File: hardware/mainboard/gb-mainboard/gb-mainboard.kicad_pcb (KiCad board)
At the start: 2 copper layers, 77.4 x 81 mm, 0 parts

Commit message: .
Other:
- net class Default: trace_width 0.25 -> 0.15

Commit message: started placing some components
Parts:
- added BRD101: POLOLU-2130, BOARD:POLOLU-2130, F.Cu at (129.1, 78.4)
- added P101: NUCLEO-CN7, CONNECTOR:SOCKET_20x2_2.54-WE-61304021821, F.Cu at (159.3, 92.3)
- added P102: NUCLEO-CN10, CONNECTOR:SOCKET_20x2_2.54-WE-61304021821, F.Cu at (98.4, 92.3)
- added P103: MOTOR_SX, CONNECTOR_MPT:CONN-MPT0.5_2-2.54, F.Cu at (115.0, 78.7)
- added P104: MOTOR_DX, CONNECTOR_MPT:CONN-MPT0.5_2-2.54, F.Cu at (142.6, 78.7)
- added P105: WE-632723300011, CONNECTOR:USB3.1-C_WE-632723300011, F.Cu at (139.8, 130.2)
- added U101: ESP32-WROOM-32E(8MB), WIFI:ESP32-WROOM-32D, F.Cu at (113.5, 125.5)
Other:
- outline, holes or cut-outs redrawn

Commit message: .
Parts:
- moved BRD101 0.49 mm to (128.7, 78.7), turned to 0 degrees
- moved P104 0.38 mm to (142.9, 78.7)
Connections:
- P103 pad 1: Net-(P103-Pad1) -> Net-(BRD101-Pad14)
- P103 pad 2: Net-(P103-Pad2) -> Net-(BRD101-Pad13)
- P104 pad 1: Net-(P104-Pad1) -> Net-(BRD101-Pad11)
- P104 pad 2: Net-(P104-Pad2) -> Net-(BRD101-Pad12)
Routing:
- net Net-(BRD101-Pad13): track 0.00 -> 21.7 mm
- net Net-(BRD101-Pad12): track 0.00 -> 19.4 mm
- net Net-(BRD101-Pad14): track 0.00 -> 12.6 mm
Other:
- net class Default: trace_width 0.15 -> 0.2
- rule via_min_size: 0.4 -> 0.6

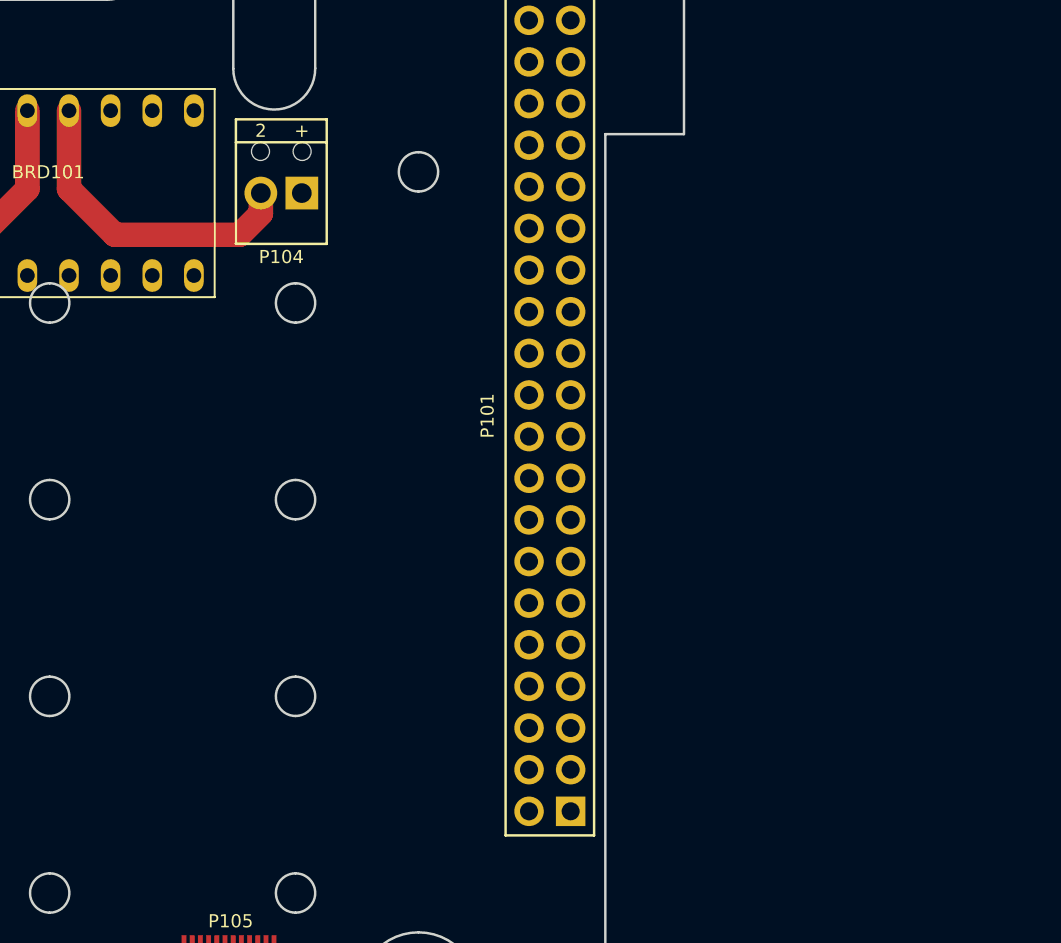
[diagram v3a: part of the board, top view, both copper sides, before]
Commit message: Working on USB: battery charger, communications and step-up
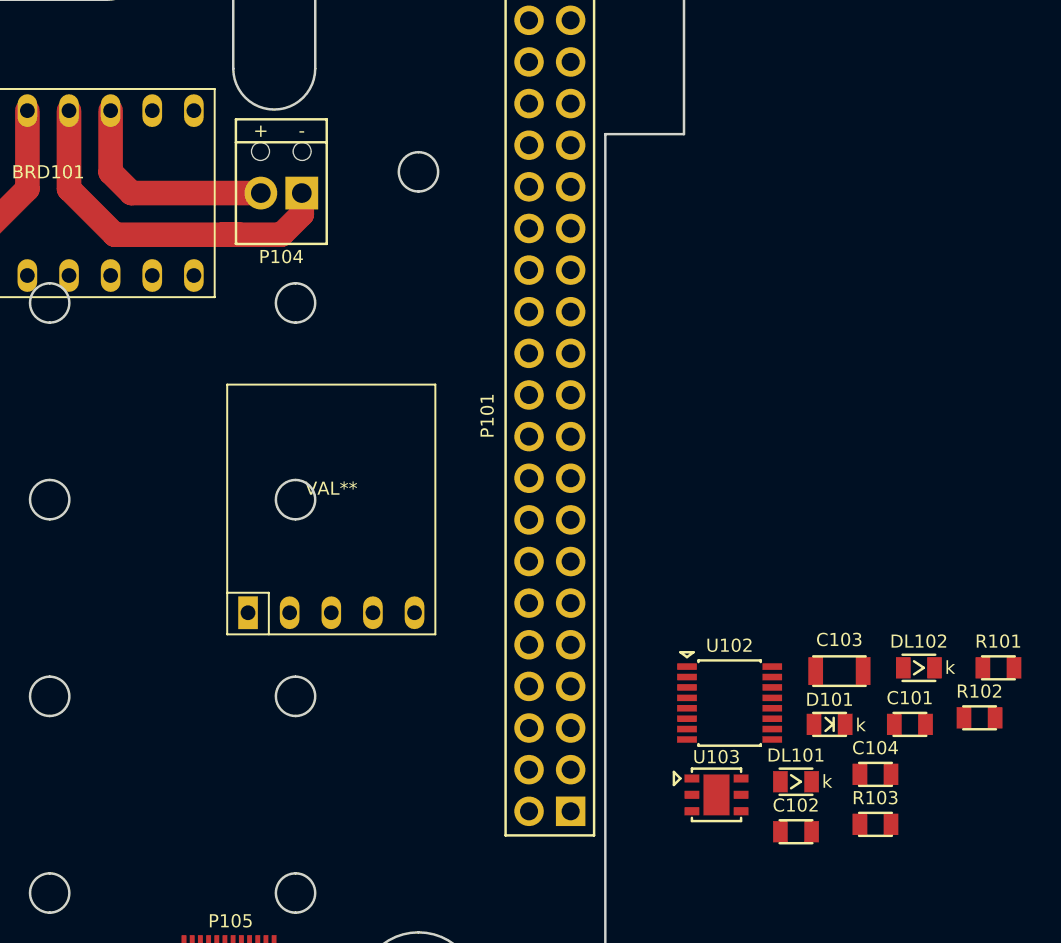
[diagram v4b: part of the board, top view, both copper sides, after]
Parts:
- added C101: 100n, CAPACITOR:CAPACITOR-0805, F.Cu at (181.3, 111.1)
- added C102: 100n, CAPACITOR:CAPACITOR-0805, F.Cu at (174.3, 117.7)
- added C103: 4u7, CAPACITOR:CAPACITOR-1206, F.Cu at (177.0, 107.9)
- added C104: 100n, CAPACITOR:CAPACITOR-0805, F.Cu at (179.2, 114.2)
- added D101: ESDA25P35, DIODE:DIODE-0805, F.Cu at (176.4, 111.1)
- added DL101: RED, LEDs:LED-0805, F.Cu at (174.3, 114.6)
- added DL102: RED, LEDs:LED-0805, F.Cu at (181.8, 107.7)
- added R101: 270, RESISTOR:RESISTOR-0805, F.Cu at (186.7, 107.7)
- added R102: 270, RESISTOR:RESISTOR-0805, F.Cu at (185.5, 110.7)
- added R103: TBD, RESISTOR:RESISTOR-0805, F.Cu at (179.2, 117.2)
- added U102: FT230XS_2, SOP:SSOP16_3.9x4.9_0.635, F.Cu at (170.3, 109.8)
- added U103: STBC08PMR, DFN:DFN6_3.0x3.0_1.0, F.Cu at (169.5, 115.4)
- added VAL**: POLOLU-2868, BOARD:POLOLU-2868, F.Cu at (146.0, 98.0)
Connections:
- P104 pad 1: Net-(BRD101-Pad11) -> Net-(BRD101-Pad12)
- P104 pad 2: Net-(BRD101-Pad12) -> Net-(BRD101-Pad11)
- P105 pad A1: Net-(P105-PadA1) -> GND
- P105 pad A12: Net-(P105-PadA12) -> GND
- P105 pad A4: Net-(P105-PadA4) -> +VUSB
- P105 pad A6: Net-(P105-PadA6) -> /USB_DP
- P105 pad A7: Net-(P105-PadA7) -> /USB_DM
- P105 pad A9: Net-(P105-PadA9) -> +VUSB
- P105 pad B1: Net-(P105-PadB1) -> GND
- P105 pad B12: Net-(P105-PadB12) -> GND
- P105 pad B4: Net-(P105-PadB4) -> +VUSB
- P105 pad B6: Net-(P105-PadB6) -> /USB_DP
- P105 pad B7: Net-(P105-PadB7) -> /USB_DM
- P105 pad B9: Net-(P105-PadB9) -> +VUSB
- P105 pad S1: Net-(P105-PadS1) -> GND
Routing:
- net Net-(BRD101-Pad11): track 0.00 -> 13.5 mm
- net Net-(BRD101-Pad12): track 19.4 -> 23.0 mm

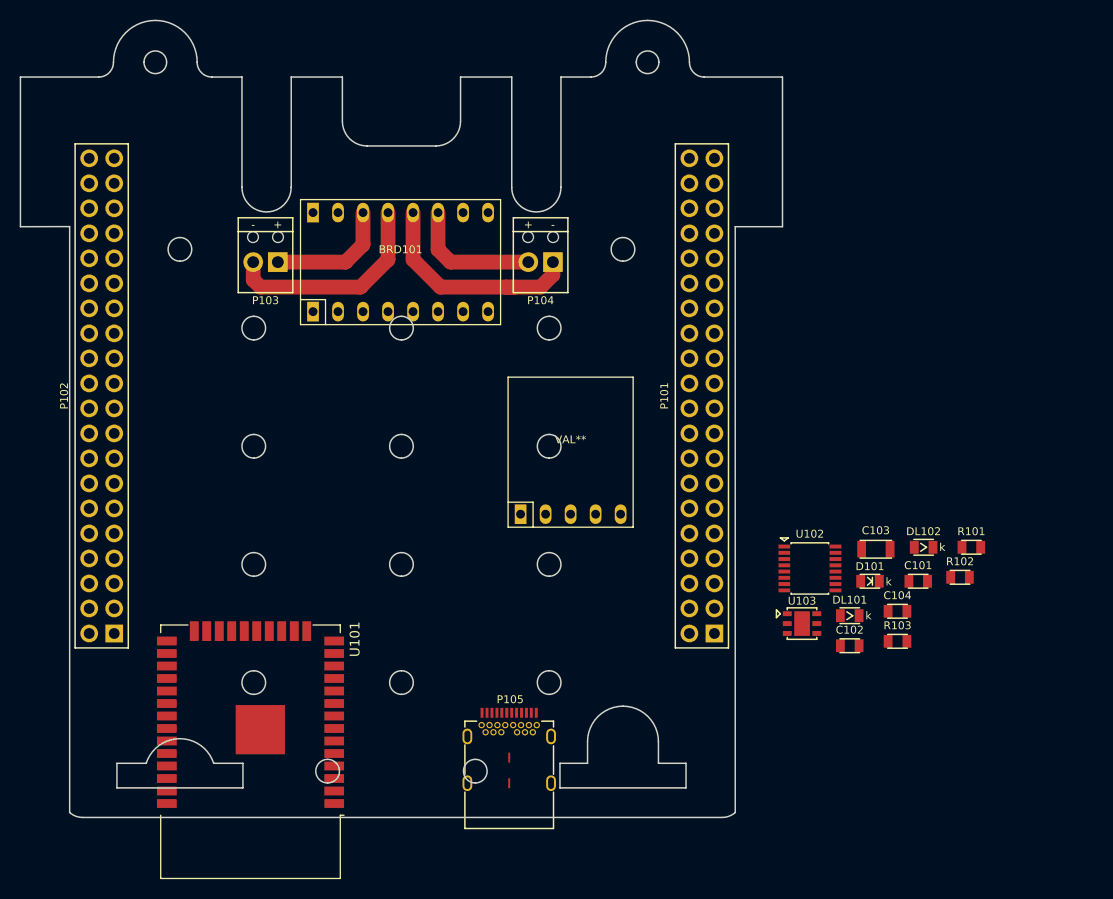
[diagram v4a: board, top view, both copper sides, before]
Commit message: motor driver connection and ESP connection.
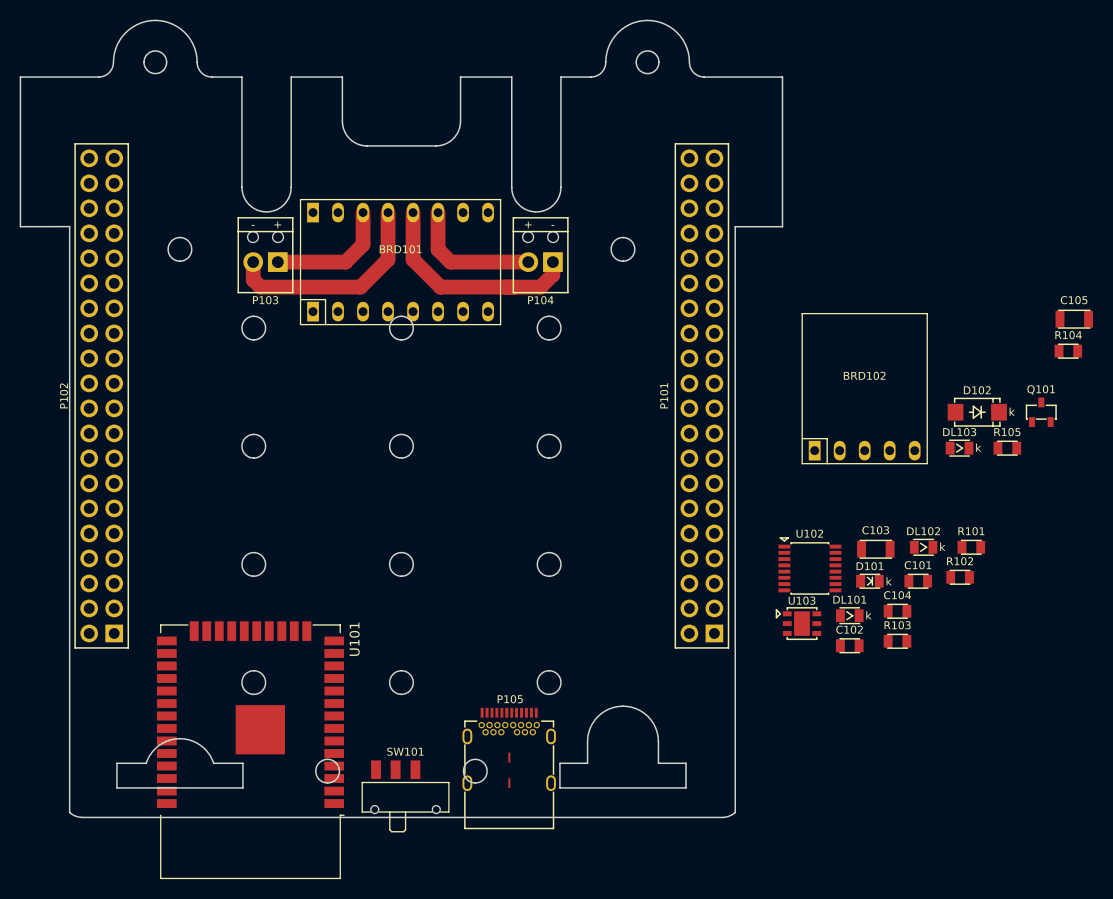
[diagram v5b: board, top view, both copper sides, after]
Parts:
- removed VAL**: POLOLU-2868, BOARD:POLOLU-2868
- added BRD102: POLOLU-2868, BOARD:POLOLU-2868, F.Cu at (175.9, 91.6)
- added C105: 4u7, CAPACITOR:CAPACITOR-1206, F.Cu at (197.1, 84.5)
- added D102: MBRA340T3G, DIODE:DIODE-DO214AC-UNI, F.Cu at (187.3, 94.0)
- added DL103: RED, LEDs:LED-0805, F.Cu at (185.5, 97.6)
- added Q101: DMP2120U-7, SOT:SOT23-3, F.Cu at (193.8, 94.0)
- added R104: 10k, RESISTOR:RESISTOR-0805, F.Cu at (196.5, 87.8)
- added R105: 330, RESISTOR:RESISTOR-0805, F.Cu at (190.3, 97.6)
- added SW101: 450405020524, SWITCH:SWITCH-SPDT-WURTH-450405020524, F.Cu at (129.2, 133.1)
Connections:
- U103 pad 1: Net-(P106-Pad1) -> +VBAT

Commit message: Working on PCB
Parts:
- added C106: 100n, CAPACITOR:CAPACITOR-0805, F.Cu at (128.1, 125.9)
- added C107: 10u, CAPACITOR:CAPACITOR-1206, F.Cu at (124.9, 132.3)
- added C108: 100n, CAPACITOR:CAPACITOR-0805, F.Cu at (127.2, 132.8)
- added C109: 100n, CAPACITOR:CAPACITOR-0805, F.Cu at (106.5, 108.8)
- added C110: 10u, CAPACITOR:CAPACITOR-1206, F.Cu at (121.0, 70.3)
- added C111: 100n, CAPACITOR:CAPACITOR-0805, F.Cu at (121.5, 68.1)
- added DL104: 155124M173200, LEDs:LEDRGB-WURTH-155124M173200, F.Cu at (159.4, 61.7)
- added DL105: 155124M173200, LEDs:LEDRGB-WURTH-155124M173200, F.Cu at (159.5, 133.2)
- added DL106: 155124M173200, LEDs:LEDRGB-WURTH-155124M173200, F.Cu at (98.4, 133.0)
- added DL107: 155124M173200, LEDs:LEDRGB-WURTH-155124M173200, F.Cu at (98.4, 61.7)
- added DL108: GREEN, LEDs:LED-0805, F.Cu at (134.1, 98.9)
- added DL109: GREEN, LEDs:LED-0805, F.Cu at (138.4, 98.9)
- added P107: EN_JMP, CONNECTOR:CONN-STRIP-2x1-2.54, F.Cu at (125.3, 127.1)
- added P108: BOOT_JMP, CONNECTOR:CONN-STRIP-2x1-2.54, F.Cu at (106.4, 111.5)
- added P109: ESP_PROG, CONNECTOR:CONN-STRIP-3x1-2.54, F.Cu at (97.1, 125.8)
- added R106: 10k, RESISTOR:RESISTOR-0805, F.Cu at (128.1, 129.2)
- added R107: TBD, RESISTOR:RESISTOR-0805, F.Cu at (155.1, 78.1)
- added R108: TBD, RESISTOR:RESISTOR-0805, F.Cu at (155.1, 74.8)
- added R109: 330, RESISTOR:RESISTOR-0805, F.Cu at (131.9, 98.9)
- added R110: 330, RESISTOR:RESISTOR-0805, F.Cu at (136.2, 98.9)
- moved R105 63.0 mm to (127.3, 98.9), turned to 270 degrees
- moved DL103 56.0 mm to (129.5, 99.0), turned to 90 degrees
- moved C105 52.9 mm to (150.9, 110.2), turned to 180 degrees
- moved R104 49.1 mm to (149.7, 102.5)
- moved BRD102 46.8 mm to (132.4, 109.0)
- moved Q101 45.5 mm to (149.7, 105.3), turned to 270 degrees
- moved D102 42.7 mm to (146.1, 105.4), turned to 90 degrees
- moved R102 41.3 mm to (144.5, 114.9), turned to 90 degrees
- moved R101 40.6 mm to (146.8, 114.8), turned to 90 degrees
- moved C102 38.9 mm to (142.1, 96.0), turned to 270 degrees
- moved DL102 37.6 mm to (144.5, 111.4), turned to 90 degrees
- moved C104 33.5 mm to (151.3, 95.7), turned to 90 degrees
- moved C101 32.3 mm to (151.3, 99.0), turned to 270 degrees
- moved C103 30.1 mm to (150.4, 122.2), turned to 180 degrees
- moved R103 29.4 mm to (149.8, 117.5), turned to 180 degrees
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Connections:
- net Net-(BRD101-Pad7) renamed /MOTOR_SLEEP
- net Net-(BRD101-Pad8) renamed /MOTOR_FAULT
- BRD101 pad 1: Net-(BRD101-Pad1) -> GND
- BRD101 pad 15: Net-(BRD101-Pad15) -> +VIN
- BRD101 pad 16: Net-(BRD101-Pad16) -> GND
- BRD101 pad 3: Net-(BRD101-Pad3) -> /MOTOR_SX_CTR1
- BRD101 pad 4: Net-(BRD101-Pad4) -> /MOTOR_SX_CTR2
- BRD101 pad 5: Net-(BRD101-Pad5) -> /MOTOR_DX_CTR2
- BRD101 pad 6: Net-(BRD101-Pad6) -> /MOTOR_DX_CTR1
- P101 pad 1: Net-(P101-Pad1) -> /LED_LX_BLUE
- P101 pad 13: Net-(P101-Pad13) -> /LED_RX_RED
- P101 pad 15: Net-(P101-Pad15) -> /LED_RX_GREEN
- P101 pad 16: Net-(P101-Pad16) -> +3.3V
- P101 pad 17: Net-(P101-Pad17) -> /LED_RX_BLUE
- P101 pad 18: Net-(P101-Pad18) -> +5V
- P101 pad 2: Net-(P101-Pad2) -> /LED_LX_RED
- P101 pad 20: Net-(P101-Pad20) -> GND
- P101 pad 22: Net-(P101-Pad22) -> GND
- P101 pad 24: Net-(P101-Pad24) -> +VIN
- P101 pad 25: Net-(P101-Pad25) -> /ESP2MCU_04
- P101 pad 27: Net-(P101-Pad27) -> /ESP2MCU_03
- P101 pad 29: Net-(P101-Pad29) -> /ESP2MCU_02
- P101 pad 31: Net-(P101-Pad31) -> /ESP2MCU_01
- P101 pad 34: Net-(P101-Pad34) -> /ADC_BAT_STATUS
- P101 pad 36: Net-(P101-Pad36) -> /UART_CMD_TX
- P101 pad 38: Net-(P101-Pad38) -> /UART_CMD_RX
- P101 pad 4: Net-(P101-Pad4) -> /LED_LX_GREEN
- P102 pad 14: Net-(P102-Pad14) -> /MOTOR_DX_CTR2
- P102 pad 21: Net-(P102-Pad21) -> /MOTOR_SX_CTR2
- P102 pad 23: Net-(P102-Pad23) -> /MOTOR_SX_CTR1
- P102 pad 25: Net-(P102-Pad25) -> /UART_DBG_TX
- P102 pad 33: Net-(P102-Pad33) -> /MOTOR_DX_CTR1
- P102 pad 34: Net-(P102-Pad34) -> /UART_DBG_RX
- U101 pad 1: Net-(U101-Pad1) -> GND
- U101 pad 15: Net-(U101-Pad15) -> GND
- U101 pad 2: Net-(U101-Pad2) -> +3.3V
- U101 pad 25: Net-(U101-Pad25) -> /ESP_BOOT
- U101 pad 26: Net-(U101-Pad26) -> /ESP2MCU_04
- U101 pad 27: Net-(U101-Pad27) -> /UART_CMD_TX
- U101 pad 28: Net-(U101-Pad28) -> /UART_CMD_RX
- U101 pad 29: Net-(U101-Pad29) -> /ESP2MCU_03
- U101 pad 3: Net-(U101-Pad3) -> /ESP_ENABLE
- U101 pad 30: Net-(U101-Pad30) -> /ESP2MCU_02
- U101 pad 31: Net-(U101-Pad31) -> /ESP2MCU_01
- U101 pad 34: Net-(U101-Pad34) -> /ESP_PROG_RX
- U101 pad 35: Net-(U101-Pad35) -> /ESP_PROG_TX
- U101 pad 38: Net-(U101-Pad38) -> GND
- U101 pad 39: Net-(U101-Pad39) -> GND
- U102 pad 1: /DEBUG_TX -> /UART_DBG_RX
- U102 pad 4: /DEBUG_RX -> /UART_DBG_TX
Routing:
- net Net-(D102-Pad2): track 0.00 -> 31.5 mm
- net Net-(BRD102-Pad3): track 0.00 -> 15.2 mm
- net +VUSB: track 0.00 -> 10.2 mm
- net /ESP_PROG_RX: track 0.00 -> 9.17 mm
- net /ESP_PROG_TX: track 0.00 -> 8.64 mm
- net Net-(DL102-Pad2): track 0.00 -> 6.13 mm
- net Net-(DL101-Pad2): track 0.00 -> 5.15 mm
- net GND: track 0.00 -> 2.15 mm
- net Net-(R103-Pad1): track 0.00 -> 1.83 mm
- net Net-(DL102-Pad1): track 0.00 -> 1.53 mm
- net Net-(DL101-Pad1): track 0.00 -> 1.47 mm
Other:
- outline, holes or cut-outs redrawn

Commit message: Working on PCB
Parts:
- added G***: LOGO, LOGO:LOGO_NOWAE_25MM_FSILK, F.Cu at (138.4, 97.9)
- added P106: BATTERY, CONNECTOR_MPT:CONN-MPT0.5_2-2.54, F.Cu at (152.5, 130.3)
- added R111: 100, RESISTOR:RESISTOR-0805, F.Cu at (154.7, 101.1)
- added R112: 100, RESISTOR:RESISTOR-0805, F.Cu at (154.8, 98.8)
- added R113: 100, RESISTOR:RESISTOR-0805, F.Cu at (154.8, 96.6)
- added R114: 100, RESISTOR:RESISTOR-0805, F.Cu at (102.6, 68.2)
- added R115: 100, RESISTOR:RESISTOR-0805, F.Cu at (104.7, 68.2)
- added R116: 100, RESISTOR:RESISTOR-0805, F.Cu at (106.9, 68.3)
- moved DL103 23.1 mm to (106.9, 103.9), turned to 180 degrees
- moved R105 21.6 mm to (106.9, 106.0), turned to 0 degrees
- moved C102 20.0 mm to (137.2, 115.4), turned to 0 degrees
- moved R109 19.8 mm to (148.9, 88.8), turned to 0 degrees
- moved DL108 19.3 mm to (148.9, 86.6), turned to 180 degrees
- moved U102 17.5 mm to (137.2, 110.7), turned to 90 degrees
- moved BRD102 17.4 mm to (116.9, 101.0), turned to 90 degrees
- moved R110 14.0 mm to (148.9, 93.1), turned to 0 degrees
- moved C104 13.8 mm to (140.3, 104.0), turned to 0 degrees
- moved DL109 13.2 mm to (148.9, 90.9), turned to 180 degrees
- moved C101 13.2 mm to (140.2, 106.2), turned to 0 degrees
- moved C103 9.27 mm to (141.2, 122.4)
- moved P105 6.48 mm to (144.0, 130.3)
- moved D101 5.65 mm to (146.2, 122.7), turned to 0 degrees
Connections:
- DL104 pad 2: /LED_RX_BLUE -> Net-(DL104-Pad2)
- DL104 pad 3: /LED_RX_GREEN -> Net-(DL104-Pad3)
- DL104 pad 4: /LED_RX_RED -> Net-(DL104-Pad4)
- DL105 pad 2: /LED_RX_BLUE -> Net-(DL104-Pad2)
- DL105 pad 3: /LED_RX_GREEN -> Net-(DL104-Pad3)
- DL105 pad 4: /LED_RX_RED -> Net-(DL104-Pad4)
- DL106 pad 2: /LED_LX_BLUE -> Net-(DL106-Pad2)
- DL106 pad 3: /LED_LX_GREEN -> Net-(DL106-Pad3)
- DL106 pad 4: /LED_LX_RED -> Net-(DL106-Pad4)
- DL107 pad 2: /LED_LX_BLUE -> Net-(DL106-Pad2)
- DL107 pad 3: /LED_LX_GREEN -> Net-(DL106-Pad3)
- DL107 pad 4: /LED_LX_RED -> Net-(DL106-Pad4)
- P101 pad 25: /ESP2MCU_04 -> Net-(P101-Pad25)
- P101 pad 27: /ESP2MCU_03 -> Net-(P101-Pad27)
- P101 pad 29: /ESP2MCU_02 -> Net-(P101-Pad29)
- P101 pad 31: /ESP2MCU_01 -> Net-(P101-Pad31)
- P101 pad 36: /UART_CMD_TX -> Net-(P101-Pad36)
- P101 pad 38: /UART_CMD_RX -> Net-(P101-Pad38)
- P102 pad 1: Net-(P102-Pad1) -> /ESP2MCU_03
- P102 pad 17: Net-(P102-Pad17) -> /UART_CMD_TX
- P102 pad 18: Net-(P102-Pad18) -> /UART_DBG_RX
- P102 pad 2: Net-(P102-Pad2) -> /ESP2MCU_01
- P102 pad 25: /UART_DBG_TX -> /UART_CMD_RX
- P102 pad 34: /UART_DBG_RX -> /UART_DBG_TX
- P102 pad 4: Net-(P102-Pad4) -> /ESP2MCU_02
- P102 pad 6: Net-(P102-Pad6) -> /ESP2MCU_04
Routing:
- net +3.3V: track 0.00 -> 235.2 mm, vias 0 -> 4
- net Net-(DL106-Pad2): track 0.00 -> 91.9 mm, vias 0 -> 2
- net /LED_LX_RED: track 0.00 -> 91.5 mm, vias 0 -> 3
- net Net-(DL106-Pad4): track 0.00 -> 91.1 mm, vias 0 -> 2
- net Net-(DL106-Pad3): track 0.00 -> 90.9 mm, vias 0 -> 2
- net Net-(DL104-Pad4): track 0.00 -> 90.9 mm, vias 0 -> 2
- net /LED_LX_BLUE: track 0.00 -> 90.7 mm, vias 0 -> 3
- net +VIN: track 0.00 -> 90.4 mm, vias 0 -> 2
- net Net-(DL104-Pad3): track 0.00 -> 89.7 mm, vias 0 -> 2
- net Net-(DL104-Pad2): track 0.00 -> 89.1 mm, vias 0 -> 2
- net /LED_LX_GREEN: track 0.00 -> 87.2 mm, vias 0 -> 3
- net /UART_DBG_TX: track 0.00 -> 74.0 mm, vias 0 -> 3
- net +VUSB: track 10.2 -> 73.2 mm, vias 0 -> 2
- net +VBAT: track 0.00 -> 58.0 mm
- net /UART_DBG_RX: track 0.00 -> 54.2 mm, vias 0 -> 3
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- added copper zone on F.Cu, net +VUSB
- added copper zone on B.Cu, net GND
- added copper zone on F.Cu, net GND
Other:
- net class Default: clearance 0.2 -> 0.15; trace_width 0.2 -> 0.15
- rule trace_clearance: 0.2 -> 0.15
- rule trace_min: 0.2 -> 0.15
- board text added: "SPONSORED BY"
